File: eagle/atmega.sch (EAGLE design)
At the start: 65 parts, among them IC1 TO 5V, IC2 LM339D, Q2 16MHz, U1 ATMEGA328P-AU

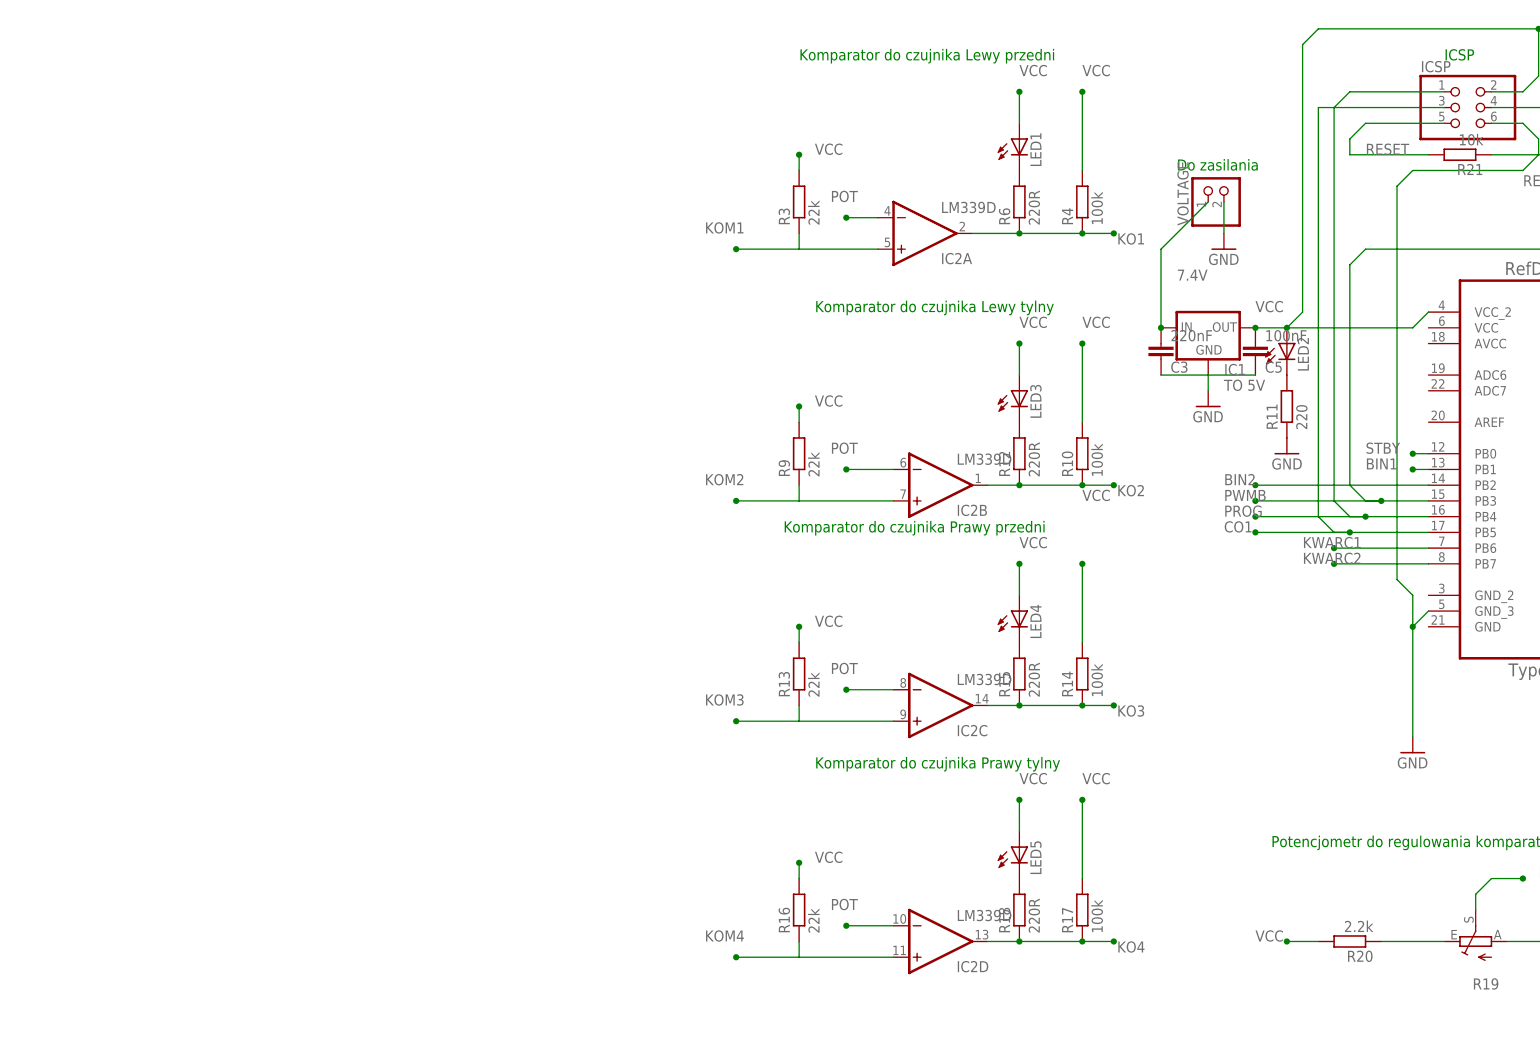
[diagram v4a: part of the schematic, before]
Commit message: Przygotowywanie do zmiany procesora.
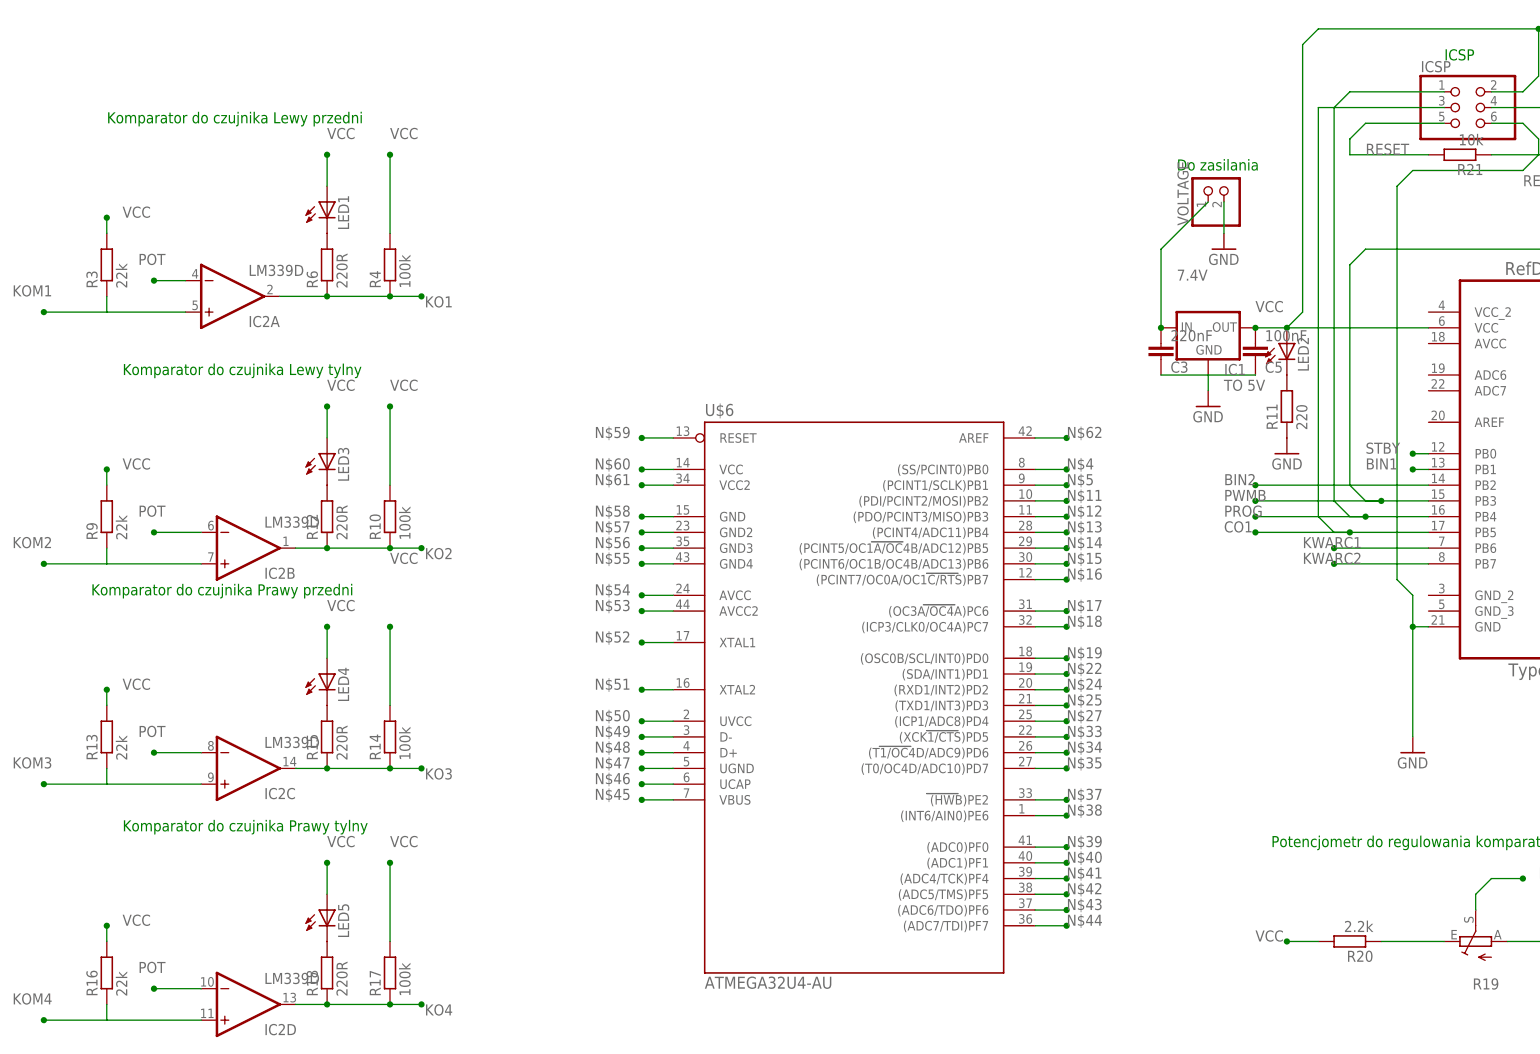
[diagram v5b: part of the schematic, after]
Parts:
- added U$6: ATMEGA32U4-AU, mega32U4:ATMEGA32U4-AU
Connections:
- new net N$11: U$6.(PDI/PCINT2/MOSI)PB2
- new net N$12: U$6.(PDO/PCINT3/MISO)PB3
- new net N$13: U$6.(PCINT4/ADC11)PB4
- new net N$14: U$6.(PCINT5/OC1A/OC4B/ADC12)PB5
- new net N$15: U$6.(PCINT6/OC1B/OC4B/ADC13)PB6
- new net N$16: U$6.(PCINT7/OC0A/OC1C/RTS)PB7
- new net N$17: U$6.(OC3A/OC4A)PC6
- new net N$18: U$6.(ICP3/CLK0/OC4A)PC7
- new net N$19: U$6.(OSC0B/SCL/INT0)PD0
- new net N$22: U$6.(SDA/INT1)PD1
- new net N$24: U$6.(RXD1/INT2)PD2
- new net N$25: U$6.(TXD1/INT3)PD3
- new net N$27: U$6.(ICP1/ADC8)PD4
- new net N$33: U$6.(XCK1/CTS)PD5
- new net N$34: U$6.(T1/OC4D/ADC9)PD6
- new net N$35: U$6.(T0/OC4D/ADC10)PD7
- new net N$37: U$6.(HWB)PE2
- new net N$38: U$6.(INT6/AIN0)PE6
- new net N$39: U$6.(ADC0)PF0
- new net N$4: U$6.(SS/PCINT0)PB0
- new net N$40: U$6.(ADC1)PF1
- new net N$41: U$6.(ADC4/TCK)PF4
- new net N$42: U$6.(ADC5/TMS)PF5
- new net N$43: U$6.(ADC6/TDO)PF6
- new net N$44: U$6.(ADC7/TDI)PF7
- new net N$45: U$6.VBUS
- new net N$46: U$6.UCAP
- new net N$47: U$6.UGND
- new net N$48: U$6.D+
- new net N$49: U$6.D-
- new net N$5: U$6.(PCINT1/SCLK)PB1
- new net N$50: U$6.UVCC
- new net N$51: U$6.XTAL2
- new net N$52: U$6.XTAL1
- new net N$53: U$6.AVCC2
- new net N$54: U$6.AVCC
- new net N$55: U$6.GND4
- new net N$56: U$6.GND3
- new net N$57: U$6.GND2
- new net N$58: U$6.GND
- new net N$59: U$6.RESET
- new net N$60: U$6.VCC
- new net N$61: U$6.VCC2
- new net N$62: U$6.AREF
- net GND: now also U1.GND; no longer U1.GND_3
- net VCC: now also U1.VCC; no longer U1.VCC_2
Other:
- moved on the sheet: IC2A, IC2B, IC2C, IC2D, LED1, LED3, LED4, LED5, R10, R12, R13, R14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

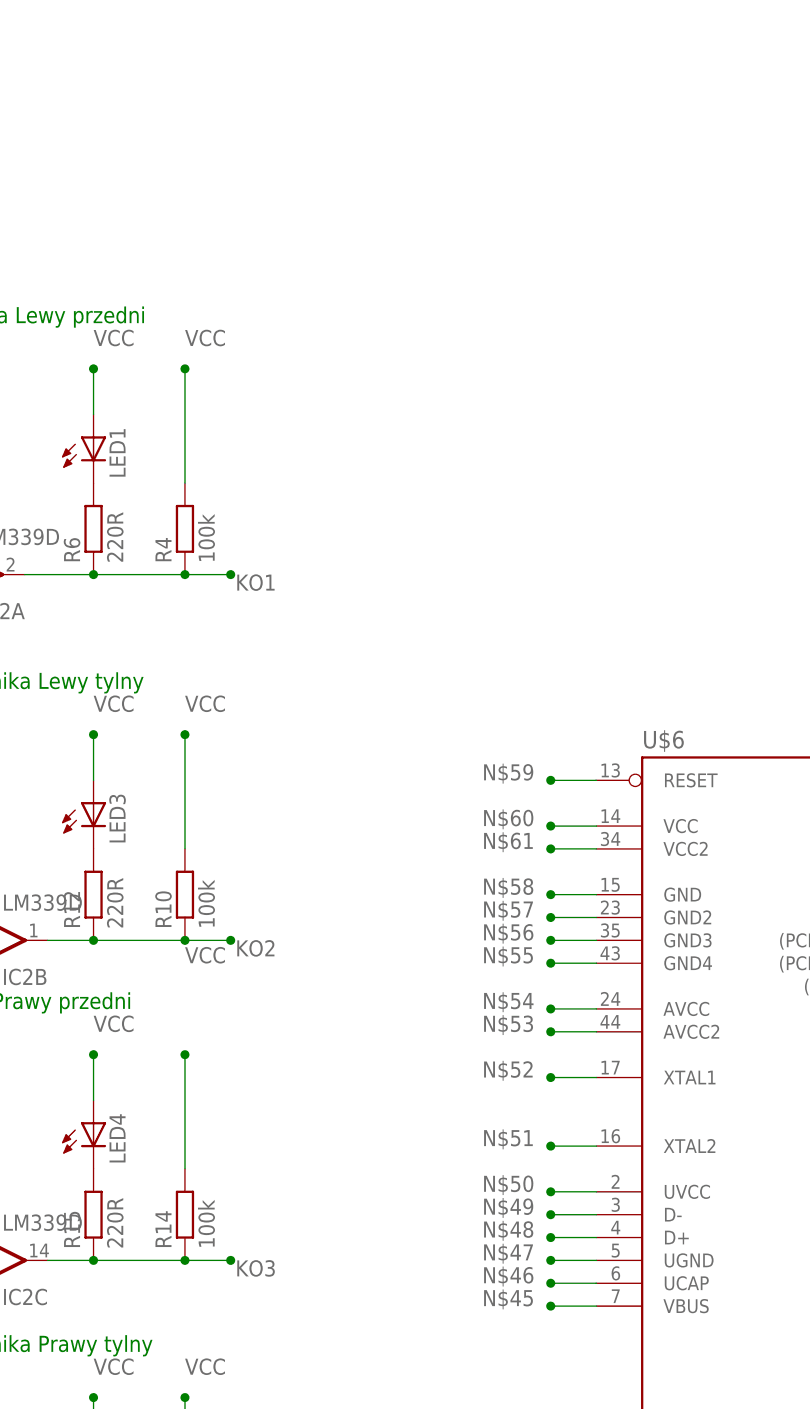
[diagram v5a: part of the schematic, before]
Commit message: Dodanie mini USB. Dodaj rezystory przed USB, podmień obudowy rezystorów.
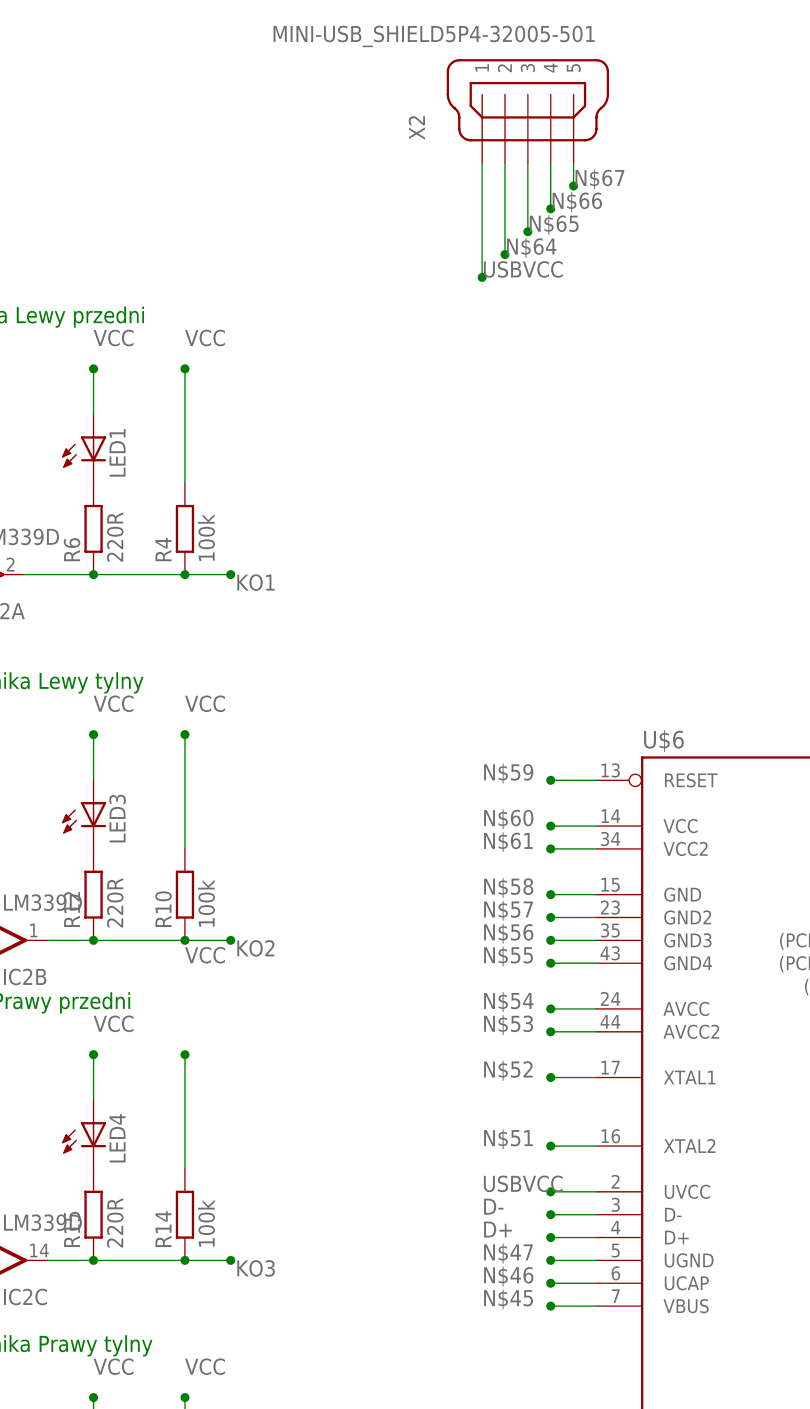
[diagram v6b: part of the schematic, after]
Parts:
- added X2: MINI-USB_SHIELD5P4-32005-501, con-cypressindustries:MINI-USB_SHIELD5P4-32005-501
- R11: device rcl:R-EU_R0805 -> resistor:R-EU_M0805
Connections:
- net N$48 renamed D+
- net N$49 renamed D-
- removed net N$50: U$6.UVCC
- new net N$64: X2G$1.2
- new net N$65: X2G$1.3
- new net N$66: X2G$1.4
- new net N$67: X2G$1.5
- new net USBVCC: U$6.UVCC, X2G$1.1
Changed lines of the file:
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@@
 <setting verticaltext="up"/>
 </settings>
-<grid distance="0.1" unitdist="inch" unit="inch" style="lines" multiple="1" display="no" altdistance="0.01" altunitdist="inch" altunit="inch"/>
+<grid distance="0.1" unitdist="inch" unit="inch" style="lines" multiple="1" display="yes" altdistance="0.01" altunitdist="inch" altunit="inch"/>
 <layers>
-<layer number="1" name="Top" color="4" fill="1" visible="no" active="no"/>
-<layer number="16" name="Bottom" color="1" fill="1" visible="no" active="no"/>
-<layer number="17" name="Pads" color="2" fill="1" visible="no" active="no"/>
-<layer number="18" name="Vias" color="2" fill="1" visible="no" active="no"/>
-<layer number="19" name="Unrouted" color="6" fill="1" visible="no" active="no"/>
-<layer number="20" name="Dimension" color="24" fill="1" visible="no" active="no"/>
-<layer number="21" name="tPlace" color="7" fill="1" visible="no" active="no"/>
-<layer number="22" name="bPlace" color="7" fill="1" visible="no" active="no"/>
-<layer number="23" name="tOrigins" color="15" fill="1" visible="no" active="no"/>
-<layer number="24" name="bOrigins" color="15" fill="1" visible="no" active="no"/>
-<layer number="25" name="tNames" color="7" fill="1" visible="no" active="no"/>
-<layer number="26" name="bNames" color="7" fill="1" visible="no" active="no"/>
-<layer number="27" name="tValues" color="7" fill="1" visible="no" active="no"/>
-<layer number="28" name="bValues" color="7" fill="1" visible="no" active="no"/>
+<layer number="1" name="Top" color="4" fill="1" visible="yes" active="no"/>
+<layer number="16" name="Bottom" color="1" fill="1" visible="yes" active="no"/>
+<layer number="17" name="Pads" color="2" fill="1" visible="yes" active="no"/>
+<layer number="18" name="Vias" color="2" fill="1" visible="yes" active="no"/>
+<layer number="19" name="Unrouted" color="6" fill="1" visible="yes" active="no"/>
+<layer number="20" name="Dimension" color="24" fill="1" visible="yes" active="no"/>
+<layer number="21" name="tPlace" color="7" fill="1" visible="yes" active="no"/>
+<layer number="22" name="bPlace" color="7" fill="1" visible="yes" active="no"/>
+<layer number="23" name="tOrigins" color="15" fill="1" visible="yes" active="no"/>
+<layer number="24" name="bOrigins" color="15" fill="1" visible="yes" active="no"/>
+<layer number="25" name="tNames" color="7" fill="1" visible="yes" active="no"/>
+<layer number="26" name="bNames" color="7" fill="1" visible="yes" active="no"/>
+<layer number="27" name="tValues" color="7" fill="1" visible="yes" active="no"/>
+<layer number="28" name="bValues" color="7" fill="1" visible="yes" active="no"/>
 <layer number="29" name="tStop" color="7" fill="3" visible="no" active="no"/>
 <layer number="30" name="bStop" color="7" fill="6" visible="no" active="no"/>
@@
 <layer number="35" name="tGlue" color="7" fill="4" visible="no" active="no"/>
 <layer number="36" name="bGlue" color="7" fill="5" visible="no" active="no"/>
-<layer number="37" name="tTest" color="7" fill="1" visible="no" active="no"/>
-<layer number="38" name="bTest" color="7" fill="1" visible="no" active="no"/>
+<layer number="37" name="tTest" color="7" fill="1" visible="yes" active="no"/>
+<layer number="38" name="bTest" color="7" fill="1" visible="yes" active="no"/>
 <layer number="39" name="tKeepout" color="4" fill="11" visible="no" active="no"/>
 <layer number="40" name="bKeepout" color="1" fill="11" visible="no" active="no"/>
@@
 <layer number="44" name="Drills" color="7" fill="1" visible="no" active="no"/>
 <layer number="45" name="Holes" color="7" fill="1" visible="no" active="no"/>
-<layer number="46" name="Milling" color="3" fill="1" visible="no" active="no"/>
-<layer number="47" name="Measures" color="7" fill="1" visible="no" active="no"/>
-<layer number="48" name="Document" color="7" fill="1" visible="no" active="no"/>
-<layer number="49" name="Reference" color="7" fill="1" visible="no" active="no"/>
-<layer number="50" name="dxf" color="7" fill="1" visible="no" active="no"/>
-<layer number="51" name="tDocu" color="7" fill="1" visible="no" active="no"/>
-<layer number="52" name="bDocu" color="7" fill="1" visible="no" active="no"/>
-<layer number="53" name="tGND_GNDA" color="7" fill="9" visible="no" active="no"/>
-<layer number="54" name="bGND_GNDA" color="1" fill="9" visible="no" active="no"/>
-<layer number="56" name="wert" color="7" fill="1" visible="no" active="no"/>
-<layer number="57" name="tCAD" color="7" fill="1" visible="no" active="no"/>
-<layer number="59" name="tCarbon" color="7" fill="1" visible="no" active="no"/>
-<layer number="60" name="bCarbon" color="7" fill="1" visible="no" active="no"/>
+<layer number="46" name="Milling" color="3" fill="1" visible="yes" active="no"/>
+<layer number="47" name="Measures" color="7" fill="1" visible="yes" active="no"/>
+<layer number="48" name="Document" color="7" fill="1" visible="yes" active="no"/>
+<layer number="49" name="Reference" color="7" fill="1" visible="yes" active="no"/>
+<layer number="50" name="dxf" color="7" fill="1" visible="yes" active="no"/>
+<layer number="51" name="tDocu" color="7" fill="1" visible="yes" active="no"/>
+<layer number="52" name="bDocu" color="7" fill="1" visible="yes" active="no"/>
+<layer number="53" name="tGND_GNDA" color="7" fill="9" visible="yes" active="no"/>
+<layer number="54" name="bGND_GNDA" color="1" fill="9" visible="yes" active="no"/>
+<layer number="56" name="wert" color="7" fill="1" visible="yes" active="no"/>
+<layer number="57" name="tCAD" color="7" fill="1" visible="yes" active="no"/>
+<layer number="59" name="tCarbon" color="7" fill="1" visible="yes" active="no"/>
+<layer number="60" name="bCarbon" color="7" fill="1" visible="yes" active="no"/>
 <layer number="88" name="SimResults" color="9" fill="1" visible="yes" active="yes"/>
 <layer number="89" name="SimProbes" color="9" fill="1" visible="yes" active="yes"/>
@@
 <part name="GND20" library="supply1" library_urn="urn:adsk.eagle:library:371" deviceset="GND" device=""/>
 <part name="GND21" library="supply1" library_urn="urn:adsk.eagle:library:371" deviceset="GND" device=""/>
-<part name="R11" library="rcl" library_urn="urn:adsk.eagle:library:334" deviceset="R-EU_" device="R0805" package3d_urn="urn:adsk.eagle:package:23553/2" value="220"/>
+<part name="R11" library="resistor" library_urn="urn:adsk.eagle:library:348" deviceset="R-EU_" device="M0805" package3d_urn="urn:adsk.eagle:package:26079/1" value="220"/>
 <part name="R2" library="rcl" library_urn="urn:adsk.eagle:library:334" deviceset="R-EU_" device="R0805" package3d_urn="urn:adsk.eagle:package:23553/2" value="220R"/>
 <part name="R5" library="rcl" library_urn="urn:adsk.eagle:library:334" deviceset="R-EU_" device="R0805" package3d_urn="urn:adsk.eagle:package:23553/2" value="220R"/>
@@
 <part name="ZWORKA" library="rcl" library_urn="urn:adsk.eagle:library:334" deviceset="R-EU_" device="0613/5V" package3d_urn="urn:adsk.eagle:package:23582/1"/>
 <part name="U$6" library="mega32U4" deviceset="ATMEGA32U4-AU" device=""/>
+<part name="X2" library="con-cypressindustries" library_urn="urn:adsk.eagle:library:138" deviceset="MINI-USB_SHIELD5P4-" device="32005-501" package3d_urn="urn:adsk.eagle:package:6463/1"/>
 </parts>
 <sheets>
@@
 <instance part="ZWORKA" gate="G$1" x="-7.62" y="63.5" rot="R90"/>
 <instance part="U$6" gate="G$1" x="-129.54" y="-5.08"/>
+<instance part="X2" gate="G$1" x="-165.1" y="104.14" rot="R90"/>
 </instances>
 <busses>
@@
 </segment>
 </net>
-<net name="N$48" class="0">
+<net name="D+" class="0">
 <segment>
 <pinref part="U$6" gate="G$1" pin="D+"/>
@@
 </segment>
 </net>
-<net name="N$49" class="0">
+<net name="D-" class="0">
 <segment>
 <pinref part="U$6" gate="G$1" pin="D-"/>
@@
 </segment>
 </net>
-<net name="N$50" class="0">
+<net name="USBVCC" class="0">
 <segment>
 <pinref part="U$6" gate="G$1" pin="UVCC"/>
@@
 <label x="-170.18" y="-15.24" size="1.778" layer="95"/>
 </segment>
+<segment>
+<pinref part="X2" gate="G$1" pin="1"/>
+<wire x1="-170.18" y1="99.06" x2="-170.18" y2="86.36" width="0.1524" layer="91"/>
+<junction x="-170.18" y="86.36"/>
+<label x="-170.18" y="86.36" size="1.778" layer="95"/>
+</segment>
 </net>
 <net name="N$51" class="0">
@@
 </segment>
 </net>
+<net name="N$64" class="0">
+<segment>
+<pinref part="X2" gate="G$1" pin="2"/>
+<wire x1="-167.64" y1="99.06" x2="-167.64" y2="88.9" width="0.1524" layer="91"/>
+<junction x="-167.64" y="88.9"/>
+<label x="-167.64" y="88.9" size="1.778" layer="95"/>
+</segment>
+</net>
+<net name="N$65" class="0">
+<segment>
+<pinref part="X2" gate="G$1" pin="3"/>
+<wire x1="-165.1" y1="99.06" x2="-165.1" y2="91.44" width="0.1524" layer="91"/>
+<junction x="-165.1" y="91.44"/>
+<label x="-165.1" y="91.44" size="1.778" layer="95"/>
+</segment>
+</net>
+<net name="N$66" class="0">
+<segment>
+<pinref part="X2" gate="G$1" pin="4"/>
+<wire x1="-162.56" y1="99.06" x2="-162.56" y2="93.98" width="0.1524" layer="91"/>
+<junction x="-162.56" y="93.98"/>
+<label x="-162.56" y="93.98" size="1.778" layer="95"/>
+</segment>
+</net>
+<net name="N$67" class="0">
+<segment>
+<pinref part="X2" gate="G$1" pin="5"/>
+<wire x1="-160.02" y1="99.06" x2="-160.02" y2="96.52" width="0.1524" layer="91"/>
+<junction x="-160.02" y="96.52"/>
+<label x="-160.02" y="96.52" size="1.778" layer="95"/>
+</segment>
+</net>
